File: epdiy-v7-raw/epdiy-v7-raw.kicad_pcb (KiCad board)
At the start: 4 copper layers, 128.4 x 74.9 mm, 113 parts, among them CN1 WP27D-S050VA3-R15000, IC1 MPU-6500, J1 USB_C_Receptacle_USB2.0, J2 EXTENSION_HEADER, J3 SIGNALS_HEADER, J5 S2B-PH-SM4-TB_LF__SN_, J6 THD2528-11SD-GF, Q1 AO3401A, SW1 TC-0522C-1.7-160G, SW3 K2-1806SQ-A2DW-04, SW4 K2-1806SQ-A2DW-04, SW5 K2-1806SQ-A2DW-04, U1 RT9080-33GJ5, U10 ED060XC5, U11 TP4056, U3 TPS651851RSLR, U4 USBLC6-2P6, U8 ESP32-S3-WROOM-1, Y1 RV-3032-C7

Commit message: 1.1 cleanup
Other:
- board text added: "BOOT/IO0"
- board text removed: "IO0"
- board text removed: "IO1"
- board text removed: "IO2"
- board text removed: "IO3"
- board text removed: "IO46"
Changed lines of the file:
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@@
 		(tags "resistor")
 		(property "Reference" "R12"
-			(at -0.01 1.24 0)
+			(at 3.26 0.08 0)
 			(layer "F.SilkS")
 			(effects
@@
 		)
 		(property "Value" "10k"
-			(at 0 1.17 360)
+			(at 0 1.17 0)
 			(layer "F.Fab")
 			(effects
@@
 		)
 		(fp_text user "${REFERENCE}"
-			(at 0 0 360)
+			(at 0 0 0)
 			(layer "F.Fab")
 			(effects
@@
 		)
 	)
-	(gr_text "IO1"
-		(at 81.5775 53.55 90)
-		(layer "F.SilkS")
-		(effects
-			(font
-				(size 1 1)
-				(thickness 0.2)
-			)
-			(justify right)
-		)
-	)
 	(gr_text "ED052TC4"
 		(at 154.375 72.325 90)
@@
 	)
 	(gr_text "SDA (39)"
-		(at 169.1 111.577381 90)
+		(at 171.64 111.577381 90)
 		(layer "F.SilkS")
 		(effects
@@
 		)
 	)
-	(gr_text "IO46"
-		(at 89.235 53.55 90)
-		(layer "F.SilkS")
-		(effects
-			(font
-				(size 1 1)
-				(thickness 0.2)
-			)
-			(justify right)
-		)
-	)
 	(gr_text "EVI"
 		(at 94.65 88.6 0)
@@
 		)
 	)
-	(gr_text "GND"
-		(at 104.55 53.55 90)
+	(gr_text "SCL (40)"
+		(at 169.04 111.625 90)
 		(layer "F.SilkS")
 		(effects
@@
 		)
 	)
-	(gr_text "SCL (40)"
-		(at 171.625 111.625 90)
-		(layer "F.SilkS")
+	(gr_text "BOOT/IO0"
+		(at 174.88 111.69 0)
+		(layer "F.SilkS" knockout)
 		(effects
 			(font
 				(size 1 1)
-				(thickness 0.2)
+				(thickness 0.14)
 			)
-			(justify right)
+			(justify left bottom)
 		)
 	)
@@
 		)
 	)
-	(gr_text "IO3"
-		(at 86.6825 53.55 90)
-		(layer "F.SilkS")
-		(effects
-			(font
-				(size 1 1)
-				(thickness 0.2)
-			)
-			(justify right)
-		)
-	)
 	(gr_text "MODE"
 		(at 178.19 79.95 0)
@@
 		)
 	)
-	(gr_text "3.3V"
-		(at 101.9975 53.55 90)
-		(layer "F.SilkS")
-		(effects
-			(font
-				(size 1 1)
-				(thickness 0.2)
-			)
-			(justify right)
-		)
-	)
 	(gr_text "34"
 		(at 169.2 77 90)
@@
 		)
 	)
-	(gr_text "IO0"
-		(at 91.7875 53.55 90)
-		(layer "F.SilkS")
-		(effects
-			(font
-				(size 1 1)
-				(thickness 0.2)
-			)
-			(justify right)
-		)
-	)
-	(gr_text "IO2"
-		(at 84.13 53.55 90)
-		(layer "F.SilkS")
-		(effects
-			(font
-				(size 1 1)
-				(thickness 0.2)
-			)
-			(justify right)
-		)
-	)
 	(gr_text "GND"
 		(at 164.05 115.339287 90)
@@
 			)
 			(justify right)
-		)
-	)
-	(gr_text "3.3V"
-		(at 79.025 53.55 90)
-		(layer "F.SilkS")
-		(effects
-			(font
-				(size 1 1)
-				(thickness 0.2)
-			)
-			(justify right)

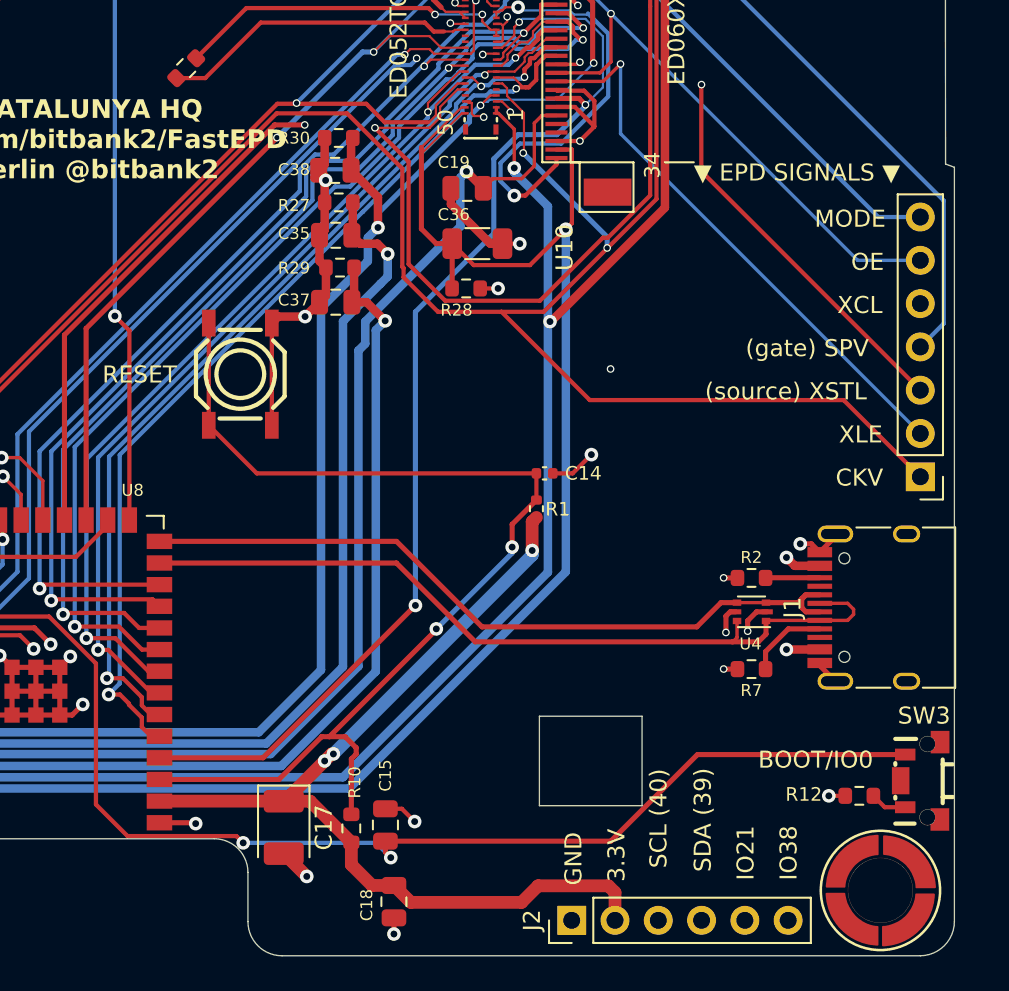
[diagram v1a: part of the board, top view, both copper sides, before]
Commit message: Add single buffer to XCL to decouple when EPD_VDD is low
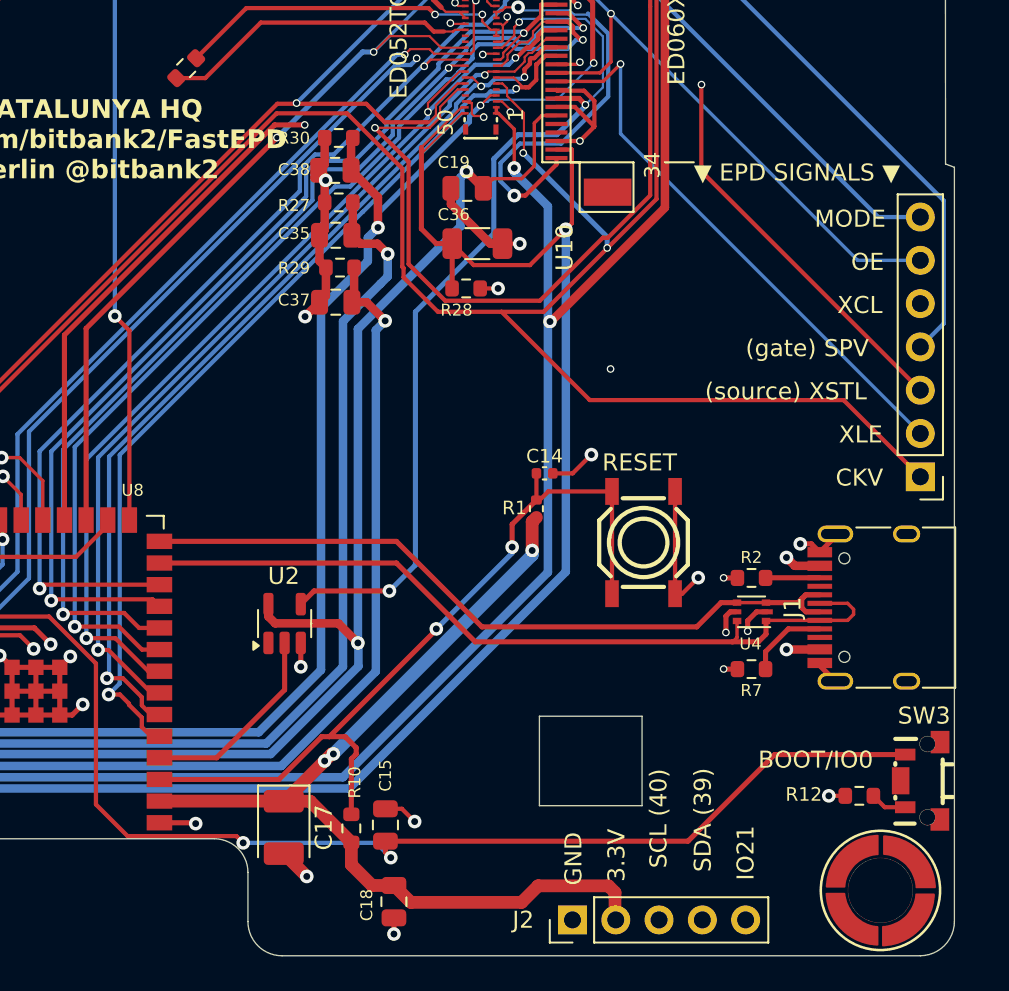
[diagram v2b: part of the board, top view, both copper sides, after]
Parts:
- added U2: 74LVC1G34, Package_TO_SOT_SMD:SOT-23-5, F.Cu at (147.1, 103.1)
- J2: footprint Connector_PinHeader_2.54mm:PinHeader_1x06_P2.54mm_Vertical -> Connector_PinHeader_2.54mm:PinHeader_1x05_P2.54mm_Vertical
- moved SW1 25.6 mm to (168.2, 98.4)
- moved J2 0.05 mm to (164.0, 120.5)
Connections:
- U8 pad 4: /XCL -> /XCL_SIG
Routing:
- net IMU_INT: track 83.4 -> 24.3 mm
- net /EN: track 63.8 -> 48.0 mm
- net /XCL: track 92.0 -> 78.6 mm
- net /XCL_SIG: track 0.00 -> 11.7 mm
- net EPD_VDD: track 129.6 -> 136.3 mm, vias 4 -> 5
- net GND: track 202.2 -> 203.3 mm, vias 100 -> 102
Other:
- board text removed: "IO38"

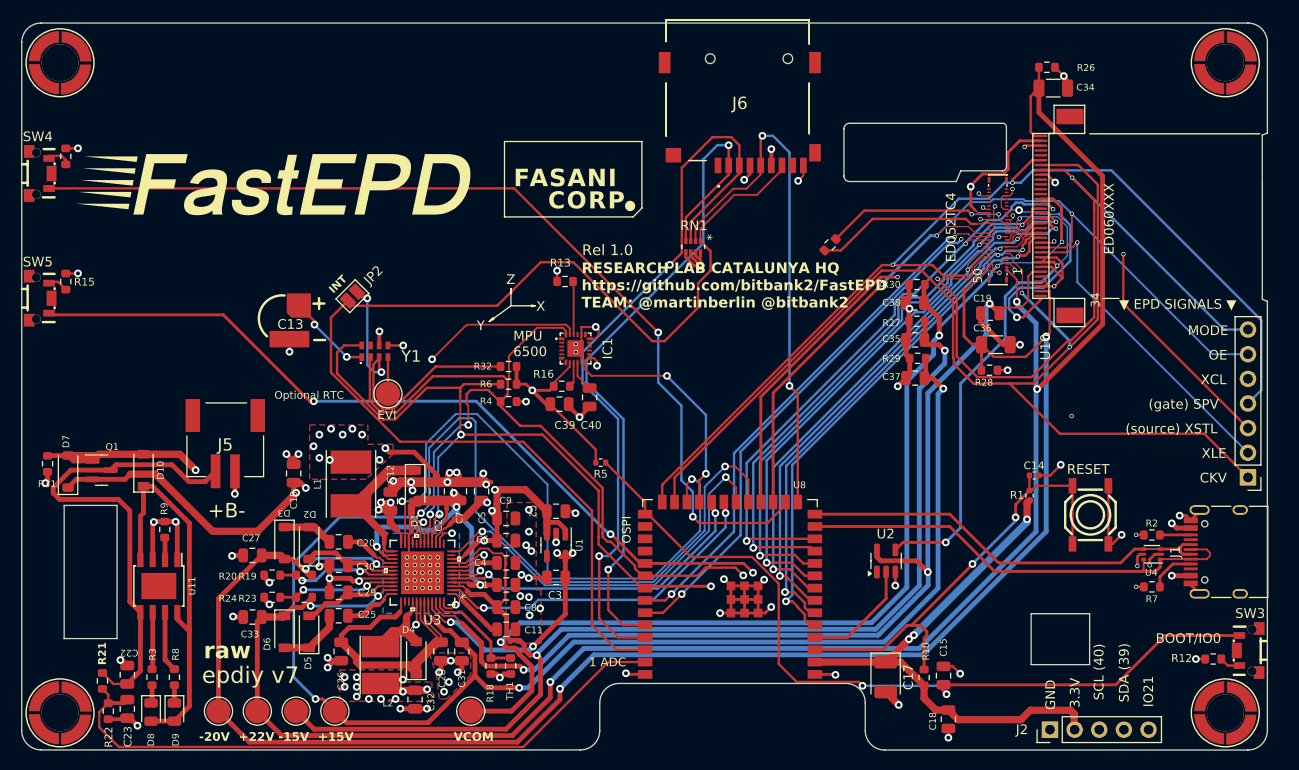
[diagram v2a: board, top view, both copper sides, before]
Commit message: Add v7 raw to epdiy
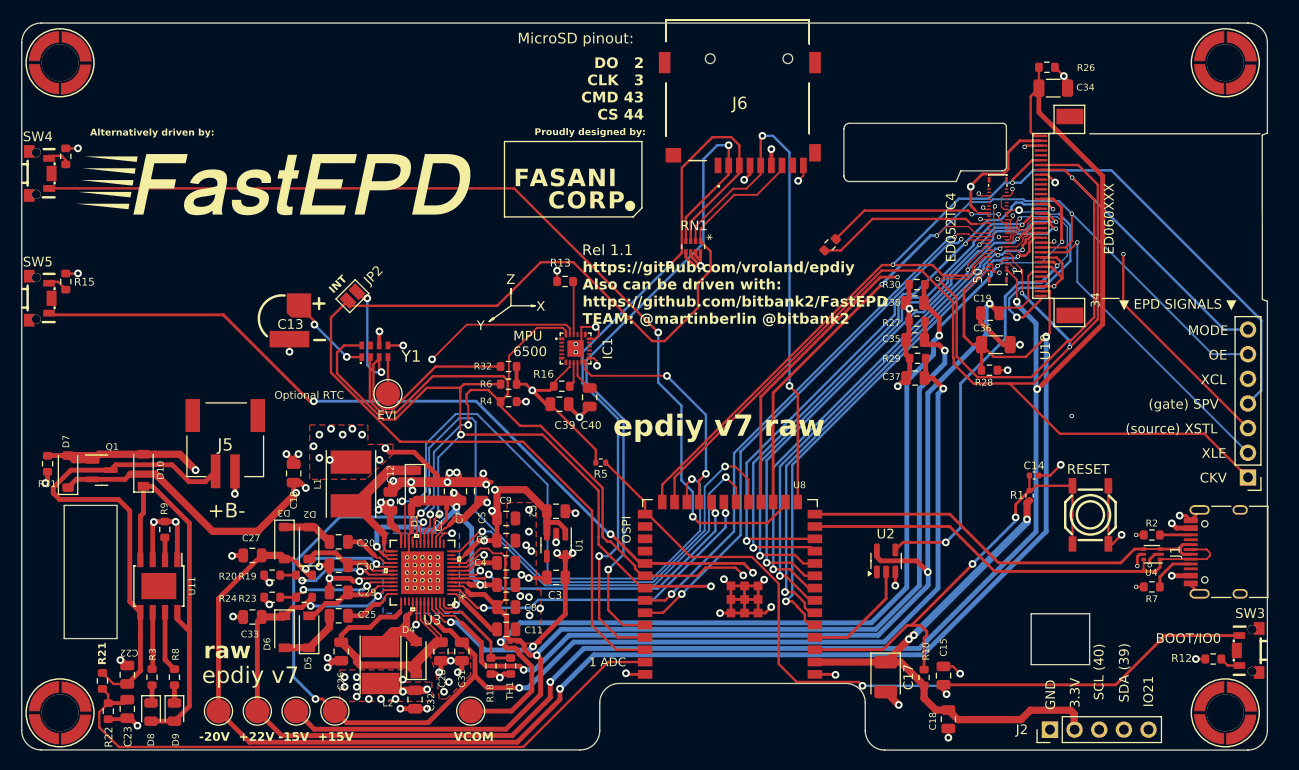
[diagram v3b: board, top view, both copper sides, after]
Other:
- board text added: "Alternatively driven by:"
- board text added: "DO 2 CLK 3 CMD 43 CS 44"
- board text added: "MicroSD pinout:"
- board text added: "Proudly collaborating with epdiy since 2022"
- board text added: "Proudly designed by:"
- board text added: "Rel 1.1"
- board text added: "based in epdiy v7 by Valentin Roland 2025 Thanks to all the contributors! For sources and documentation visit https://github.com/vroland/epdiy"
- board text added: "epdiy v7 raw"
- board text added: "https://github.com/vroland/epdiy Also can be driven with: https://github.com/bitbank2/FastEPD TEAM: @martinberlin @bitbank2"
- board text removed: "RESEARCH LAB CATALUNYA HQ https://github.com/bitbank2/FastEPD TEAM: @martinberlin @bitbank2"
- board text removed: "Rel 1.0"
- board text removed: "based in epdiy v7 by Valentin Roland 2023 Thanks to all the contributors! For sources and documentation visit https://github.com/bitbank2/FastEPD"
